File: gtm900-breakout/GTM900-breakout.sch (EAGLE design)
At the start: 94 parts, among them J1 AUDIO-JACK3, K1 694108106102, T1 BC847, T2 BC847, T3 BC847, T4 BC847, U1 FH12A-40S-0.5SH(55), U2 MCP1827T-ADJE/ET, U3 MIC5366, U4 CP2105-GM, U5 IP4234CZ6, X4 MINI-USB-SHIELD-UX60-MB-5ST

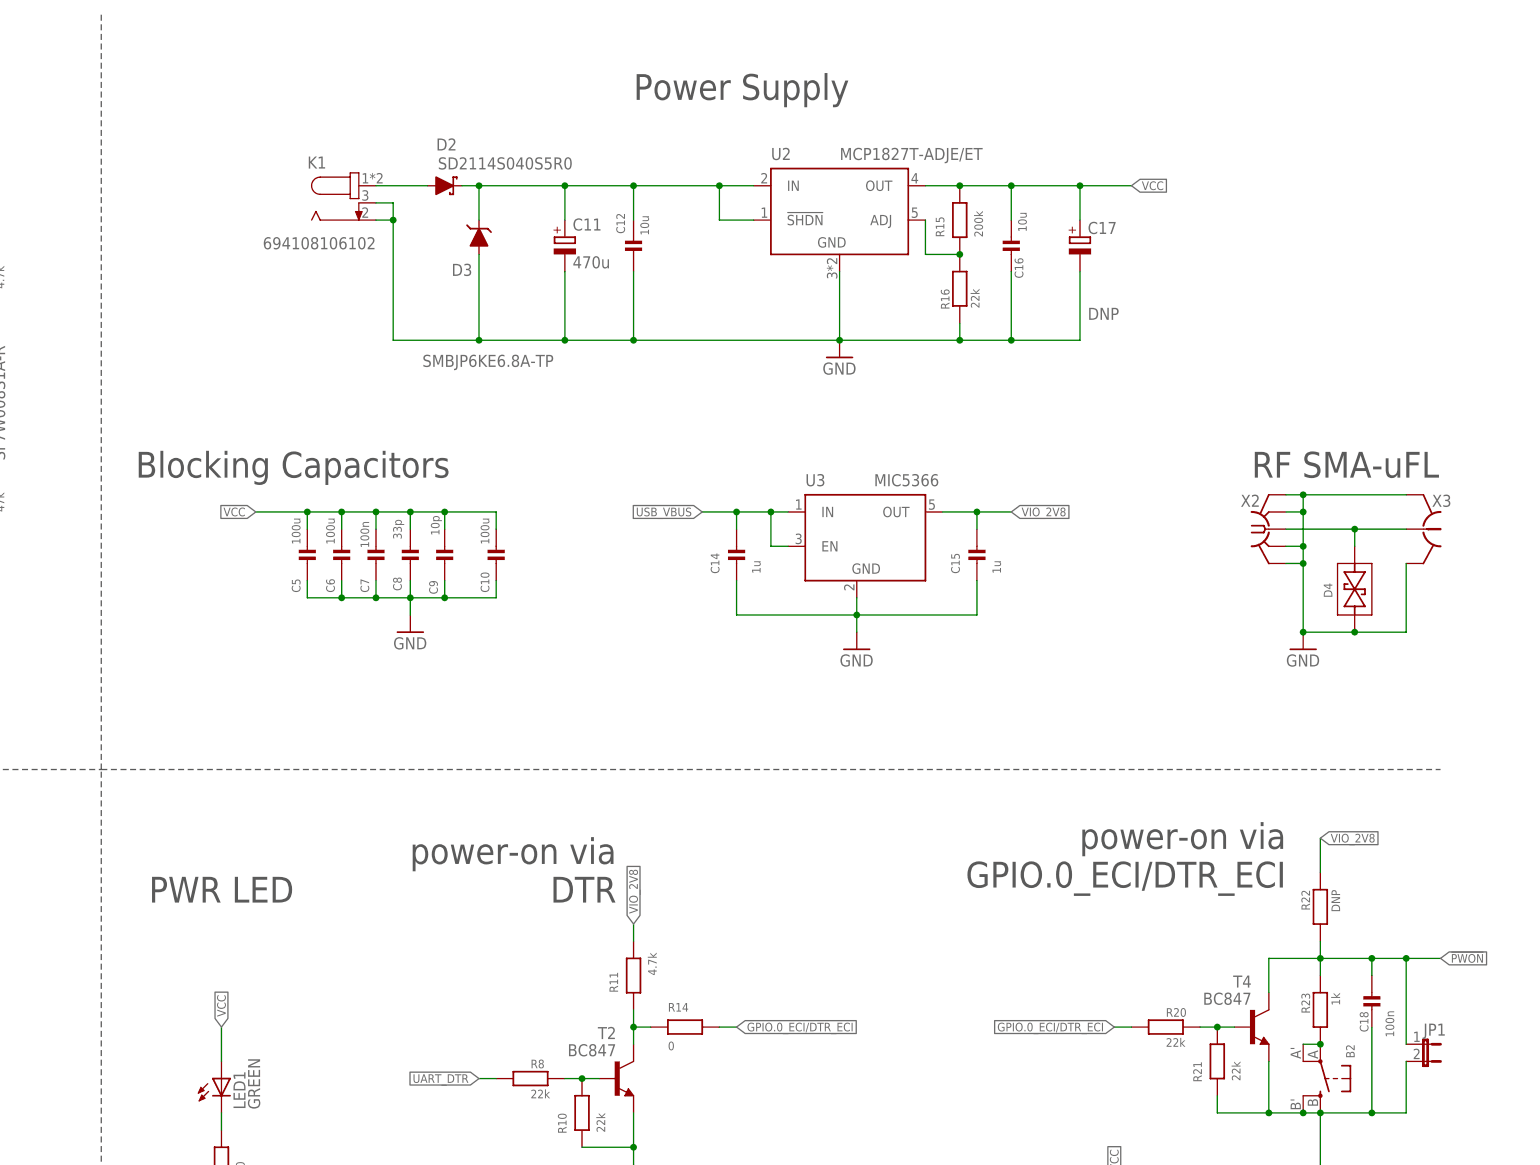
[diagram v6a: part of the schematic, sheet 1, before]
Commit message: gtm900-bo: add header for power source selection (DC in / USB)
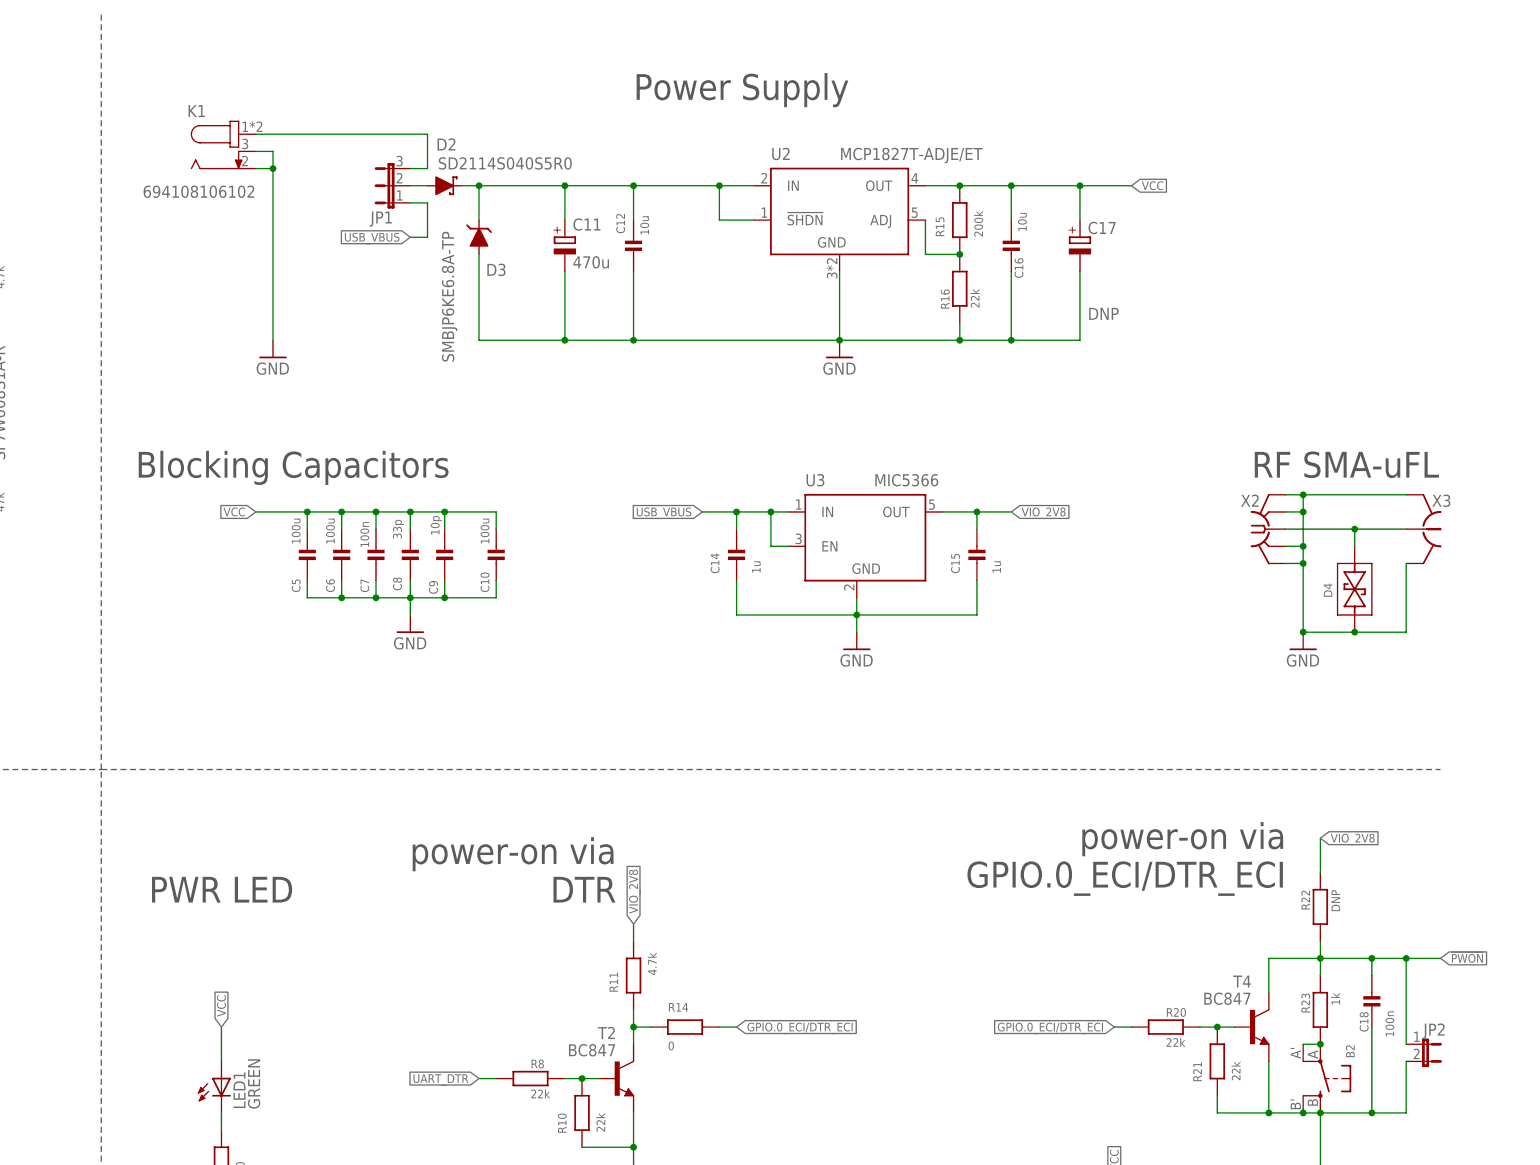
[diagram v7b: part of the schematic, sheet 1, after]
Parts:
- added JP3: (no value), microbuilder:HEADER-1X476MIL
- JP1: device jumper:JP1E -> jumper:JP2E
- JP2: device microbuilder:HEADER-1X476MIL -> jumper:JP1E
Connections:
- new net N$19: D2.A, JP1.2
- net !PWON: now also JP2.1; no longer JP1.1
- net EAR+: now also JP3.3; no longer JP2.3
- net EAR-: now also JP3.4; no longer JP2.4
- net GND: now also JP2.2; no longer JP1.2
- net MIC+: now also JP3.1; no longer JP2.1
- net MIC-: now also JP3.2; no longer JP2.2
- net N$4: now also JP1.3; no longer D2.A
- net USB_VBUS: now also JP1.1
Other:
- moved on the sheet: K1

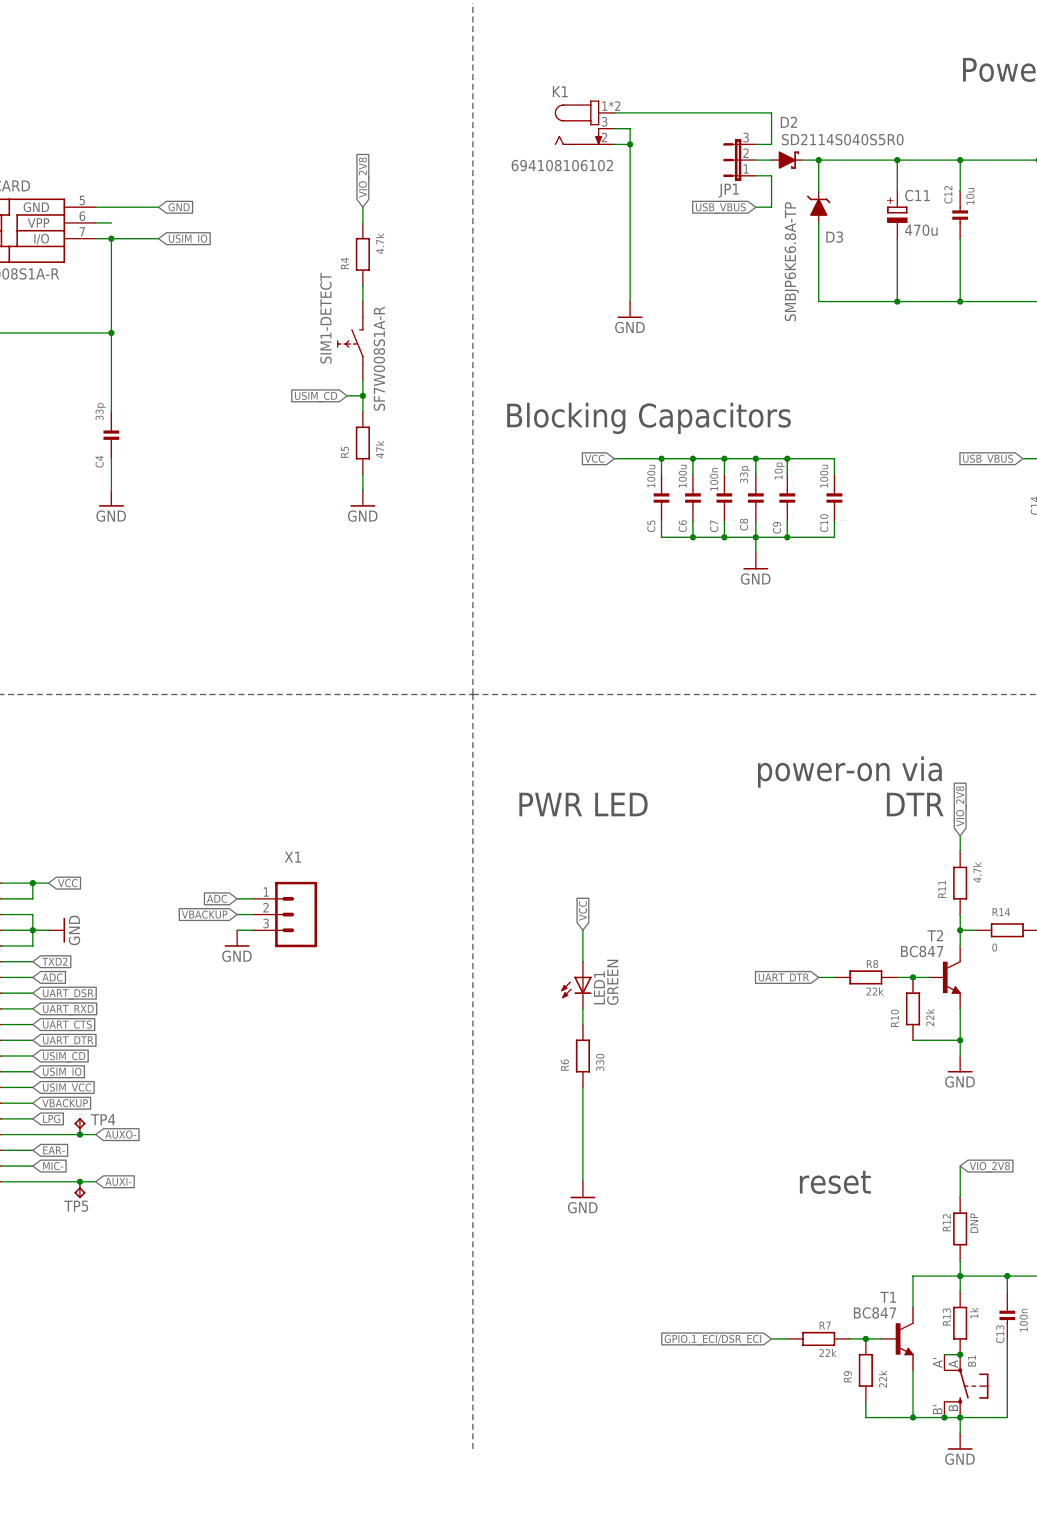
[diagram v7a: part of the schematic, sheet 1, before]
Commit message: gtm900-bo: update parts to avail @Digikey, upd all ext'd attribs
... in sch and brd too
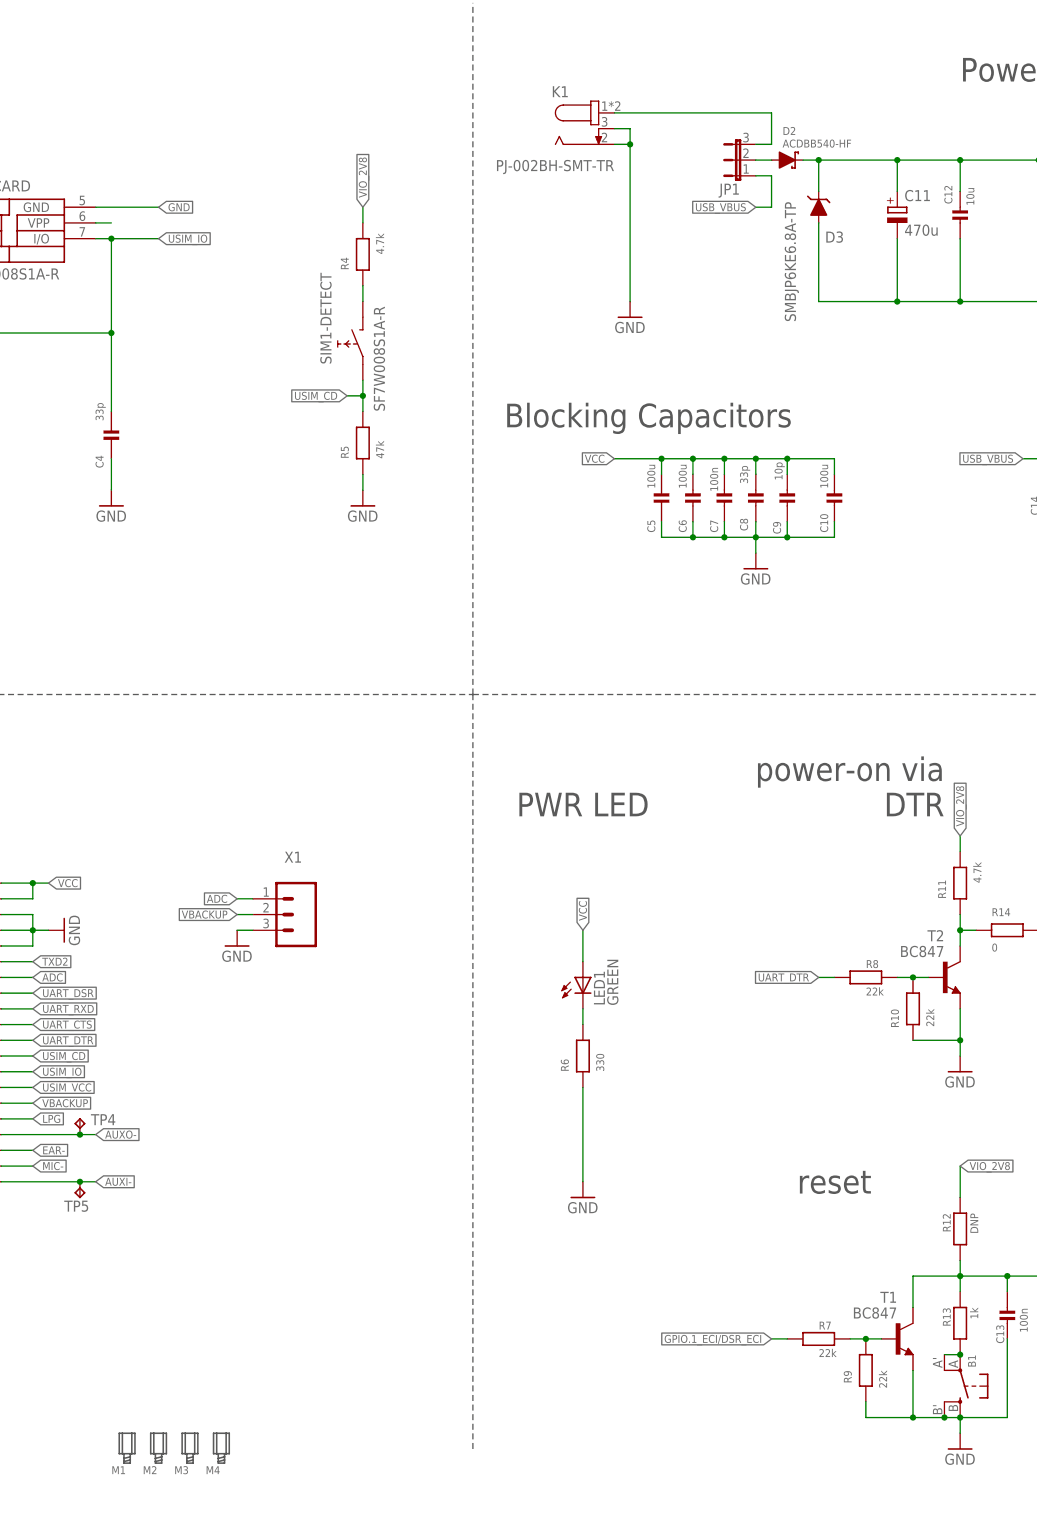
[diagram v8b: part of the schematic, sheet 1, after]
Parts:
- B1, B2: CLASS UNKNOWN CLASS -> TACT SWITCH; DESCRIPTION NO DESCRIPTION -> SWITCH TACTILE SPST-NO 0.02A 15V; LINK UNKNOWN LINK -> https://www.digikey.de/product-detail/de/panasonic-electron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; MANUFACTURER UNKNOWN MANUFACTURER -> Panasonic Electronic Components; MANUFACTURERPARTNUMBER UNKNOWN MANUFACTURER PART NUMBER -> EVQ-Q2M03W; SOURCE UNKNOWN SOURCE -> DIGIKEY; SOURCEPARTNUMBER UNKNOWN SOURCE PART NUMBER -> P12946SCT-ND
- C1, C13, C18, C7: LINK http://www.digikey.com/product-detail/en/foo/1276-1005-1-ND -> http://www.digikey.de/product-detail/de/foo/1276-1005-1-ND
- C10, C5, C6: DESCRIPTION 100µF 6.3V Ceramic Capacitor X5R 1206 (3216 Metric) 0.126" 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 -> CAP CER 100UF 6.3V X5R 1206; LINK http://www.digikey.com/product-detail/en/murata-electronics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 -> http://www.digikey.de/product-detail/de/murata-electronics-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; MANUFACTURER Murata Electronics North America -> Murata Electronics
- C11: DESCRIPTION 470µF 6.3V Aluminum Capacitors Radial, Can - SMD 2000 Hrs @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 -> CAP ALUM 470UF 20%% 6.3V SMD; LINK http://www.digikey.com/product-detail/en/nichicon/UUR0J471M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 -> http://www.digikey.de/product-detail/de/nichicon/UUR0J471MN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
- C12, C16, C31, C32: DESCRIPTION 10µF 16V Ceramic Capacitor X5R 0805 (2012 Metric) 0.079" L 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 -> CAP CER 10UF 16V X5R 0805; LINK http://www.digikey.com/product-detail/en/samsung-electro-me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 -> https://www.digikey.de/product-detail/de/murata-electronics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; MANUFACTURER Samsung Electro-Mechanics America, Inc. -> Murata Electronics; MANUFACTURERPARTNUMBER CL21A106KOQNNNG -> GRM21BR61C106KE15K; SOURCEPARTNUMBER 1276-6455-1-ND -> 490-6473-1-ND
- C14, C15, C20: DESCRIPTION 1µF 16V Ceramic Capacitor X5R 0603 (1608 Metric) 0.063" L x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 -> CAP CER 1UF 16V X5R 0603; LINK http://www.digikey.com/product-detail/en/murata-electronics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 -> https://www.digikey.de/product-detail/de/samsung-electro-me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; MANUFACTURER Murata Electronics North America -> Samsung Electro-Mechanics; MANUFACTURERPARTNUMBER GRM188R61C105KA93J -> CL10A105KO8NNNC; SOURCEPARTNUMBER 490-6412-1-ND -> 1276-1034-1-ND
- C19, C23: DESCRIPTION 4.7µF 10V Ceramic Capacitor X5R 0603 (1608 Metric) 0.063" L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 -> CAP CER 4.7UF 10V X5R 0603; LINK http://www.digikey.com/product-detail/en/samsung-electro-me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 -> https://www.digikey.de/product-detail/de/samsung-electro-me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; MANUFACTURER Samsung Electro-Mechanics America, Inc. -> Samsung Electro-Mechanics; MANUFACTURERPARTNUMBER CL10A475KP8NNNC -> CL10A475MP8NNNC; SOURCEPARTNUMBER 1276-1044-1-ND -> 1276-1905-1-ND
- C2, C25, C26, C27, C28, C29, C3, C30, C33, C34, C4, C8: LINK http://www.digikey.com/product-detail/en/CL05C330JB5NNNC/12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 -> http://www.digikey.de/product-detail/de/CL05C330JB5NNNC/127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
- C21, C22, C24: DESCRIPTION 0.10µF 16V Ceramic Capacitor X5R 0201 (0603 Metric) 0.024" 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 -> CAP CER 0.1UF 16V X5R 0201; LINK http://www.digikey.com/product-detail/en/murata-electronics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 -> http://www.digikey.de/product-detail/de/murata-electronics-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; MANUFACTURER Murata Electronics North America -> Murata Electronics
- C9: LINK http://www.digikey.com/product-detail/en/C0603C100J5GACTU/3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 -> http://www.digikey.de/product-detail/de/C0603C100J5GACTU/39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
- D2: value SD2114S040S5R0 -> ACDBB540-HF; DESCRIPTION DIODE SCHOTTKY 40V 5A SMB -> DIODE SCHOTTKY 40V 5A DO214AA; LINK https://www.digikey.de/product-detail/de/avx-corporation/SD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 -> https://www.digikey.de/product-detail/de/comchip-technology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; MANUFACTURER AVX Corporation -> Comchip Technology; MANUFACTURERPARTNUMBER SD2114S040S5R0 -> ACDBB540-HF; SOURCEPARTNUMBER 478-7816-1-ND -> 641-1898-2-ND
- D4: DESCRIPTION TVS DIODE 5V 10V 0402 -> TVS DIODE 5V 15.5V 0402; LINK https://www.digikey.de/product-detail/de/avx-corporation/GG040205170N2P/478-10595-1-ND/ -> https://www.digikey.de/product-detail/de/avx-corporation/GG0402050R3C2P/478-10591-1-ND; MANUFACTURERPARTNUMBER GG040205170N2P -> GG0402050R3C2P; ROHSCERTIFICATE Bleifrei / RoHS-konform -> UNKNOWN ROHS CERTIFICATE; SOURCEPARTNUMBER 478-10595-1-ND -> 478-10591-1-ND
- J1: CLASS (none) -> CONNECTOR; DESCRIPTION (none) -> AUDIO JACK, 3.5 MM, RT, 4 CONDUC; LINK (none) -> https://www.digikey.de/product-detail/de/cui-devices/SJ2-35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; MANUFACTURER (none) -> CUI Devices; MANUFACTURERPARTNUMBER (none) -> SJ2-3574A-SMT-TR; POPULATED (none) -> TRUE; ROHSCERTIFICATE (none) -> UNKNOWN ROHS CERTIFICATE; SOURCE (none) -> DIGIKEY; SOURCEPARTNUMBER (none) -> CP-SJ2-3574A-SMT-CT-ND
- K1: value 694108106102 -> PJ-002BH-SMT-TR; CLASS RELAY -> CONNECTOR; DESCRIPTION Power Barrel Connector Jack 2.50mm ID (0.098"), 5.50mm OD (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 -> CONN PWR JACK 2.5X5.5MM SOLDER; LINK http://www.digikey.com/product-detail/en/wurth-electronics-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 -> https://www.digikey.de/product-detail/de/cui-inc/PJ-002BH-S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; MANUFACTURER Wurth Electronics Inc -> CUI Devices; MANUFACTURERPARTNUMBER 694108106102 -> PJ-002BH-SMT-TR; SOURCEPARTNUMBER 732-5933-1-ND -> CP-002BHPJCT-ND
- R10, R16, R17, R18, R20, R21, R7, R8, R9: DESCRIPTION RES 22K OHM 1/10W 1% 0603 SMD -> RES SMD 22K OHM 1%% 1/10W 0603; LINK http://www.digikey.de/product-detail/de/MCR03ERTF2202/RHM22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 -> https://www.digikey.de/product-detail/de/yageo/RC0603FR-072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; MANUFACTURER Rohm Semiconductor -> Yageo; MANUFACTURERPARTNUMBER MCR03ERTF2202 -> RC0603FR-0722KL; ROHSCERTIFICATE Bleifrei / RoHS-konform -> UNKNOWN ROHS CERTIFICATE; SOURCEPARTNUMBER RHM22.0KCFCT-ND -> 311-22.0KHRCT-ND
- R11, R25, R4: DESCRIPTION RES SMD 4.7K OHM 5% 1/10W 0603 -> RES SMD 4.7K OHM 5%% 1/10W 0603; LINK http://www.digikey.com/product-detail/en/yageo/RC0603JR-074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 -> http://www.digikey.de/product-detail/de/yageo/RC0603JR-074K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
- R12, R22: POPULATED TRUE -> FALSE
- R13, R23: DESCRIPTION NO DESCRIPTION -> RES SMD 1K OHM 0.5%% 1/16W 0603; LINK UNKNOWN LINK -> https://www.digikey.de/product-detail/de/susumu/RR0816P-102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; MANUFACTURER UNKNOWN MANUFACTURER -> Susumu; MANUFACTURERPARTNUMBER UNKNOWN MANUFACTURER PART NUMBER -> RR0816P-102-D; SOURCE UNKNOWN SOURCE -> DIGIKEY; SOURCEPARTNUMBER UNKNOWN SOURCE PART NUMBER -> RR08P1.0KDCT-ND
- R14, R24, R27: DESCRIPTION NO DESCRIPTION -> RES 0 OHM JUMPER 1/16W 0402; LINK http://www.digikey.de/product-detail/de/AC0402JR-070RL/311-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 -> https://www.digikey.de/product-detail/de/stackpole-electron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; MANUFACTURER UNKNOWN MANUFACTURER -> Stackpole Electronics Inc; MANUFACTURERPARTNUMBER UNKNOWN MANUFACTURER PART NUMBER -> RMCF0402ZT0R00; SOURCE UNKNOWN SOURCE -> DIGIKEY; SOURCEPARTNUMBER UNKNOWN SOURCE PART NUMBER -> RMCF0402ZT0R00CT-ND
- R19, R6: DESCRIPTION RES SMD 330 OHM 5% 1/10W 0603 -> RES SMD 330 OHM 5%% 1/10W 0603; LINK http://www.digikey.com/product-detail/en/yageo/RC0603JR-073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 -> http://www.digikey.de/product-detail/de/yageo/RC0603JR-0733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
- R2, R3: DESCRIPTION RES SMD 47 OHM 5% 1/10W 0603 -> RES SMD 47 OHM 5%% 1/10W 0603; LINK http://www.digikey.com/product-detail/en/yageo/RC0603JR-074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 -> http://www.digikey.de/product-detail/de/yageo/RC0603JR-0747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
- R26: DESCRIPTION RES SMD 1M OHM 5% 1/20W 0201 -> RES SMD 1M OHM 1%% 1/10W 0603; LINK http://www.digikey.com/product-detail/en/samsung-electro-me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 -> https://www.digikey.de/product-detail/de/yageo/RC0603FR-071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; MANUFACTURER Samsung Electro-Mechanics America, Inc. -> Yageo; MANUFACTURERPARTNUMBER RC0603J105CS -> RC0603FR-071ML; SOURCEPARTNUMBER 1276-3856-1-ND -> 311-1.00MHRCT-ND
- R5: DESCRIPTION NO DESCRIPTION -> RES SMD 47K OHM 1%% 1/10W 0603; LINK https://www.digikey.de/product-detail/de/stackpole-electron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 -> https://www.digikey.de/product-detail/de/yageo/RC0603FR-074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; MANUFACTURER UNKNOWN MANUFACTURER -> Yageo; MANUFACTURERPARTNUMBER UNKNOWN MANUFACTURER PART NUMBER -> RC0603FR-0747KL; SOURCE UNKNOWN SOURCE -> DIGIKEY; SOURCEPARTNUMBER UNKNOWN SOURCE PART NUMBER -> 311-47.0KHRCT-ND
- SIM1: DESCRIPTION 8 (6 + 2) Position Card Connector SIM Card Surface Mount, R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 -> CONN SIM CARD HINGED TYPE R/A; LINK http://www.digikey.com/product-detail/en/jae-electronics/SF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 -> https://www.digikey.de/product-detail/de/jae-electronics/SF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; MANUFACTURERPARTNUMBER SF7W008S1AE900 -> SF7W008S1AR900; SOURCEPARTNUMBER 670-2337-1-ND -> 670-2985-1-ND
- T1, T2, T3, T4: CLASS UNKNOWN CLASS -> TRANSISTOR
- U1: CLASS IC -> CONNECTOR; DESCRIPTION NO DESCRIPTION -> CONN FFC TOP 40POS 0.50MM R/A; LINK UNKNOWN LINK -> https://www.digikey.de/product-detail/de/hirose-electric-co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; MANUFACTURER UNKNOWN MANUFACTURER -> Hirose Electric Co Ltd; MANUFACTURERPARTNUMBER UNKNOWN MANUFACTURER PART NUMBER -> FH12A-40S-0.5SH(55); SOURCE UNKNOWN SOURCE -> DIGIKEY; SOURCEPARTNUMBER UNKNOWN SOURCE PART NUMBER -> HFK140CT-ND
- U2: DESCRIPTION Linear Voltage Regulator IC Positive Fixed 1 Output 3.3V 3A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 -> IC REG LINEAR 3.3V 3A D2PAK; LINK http://www.digikey.com/product-detail/en/stmicroelectronics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 -> http://www.digikey.de/product-detail/de/stmicroelectronics/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
- U3: DESCRIPTION NO DESCRIPTION -> IC REG LINEAR 2.8V 150MA SC70-5; MANUFACTURER UNKNOWN MANUFACTURER -> Microchip Technology; MANUFACTURERPARTNUMBER UNKNOWN MANUFACTURER PART NUMBER -> MIC5366-2.8YC5-TR; SOURCE UNKNOWN SOURCE -> DIGIKEY; SOURCEPARTNUMBER UNKNOWN SOURCE PART NUMBER -> 576-3209-1-ND
- U4: DESCRIPTION USB Bridge, USB to UART USB 2.0 UART Interface 24-QFN (4x4) -> IC SGL USB-DL UART BRIDGE 24QFN; LINK http://www.digikey.com/product-detail/en/silicon-labs/CP210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 -> http://www.digikey.de/product-detail/de/silicon-labs/CP2105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
- U5: DESCRIPTION TVS DIODE 5.5VWM 6TSOP -> TVS DIODE 5.5V 6TSOP; LINK http://www.digikey.com/product-detail/en/nxp-semiconductors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 -> http://www.digikey.de/product-detail/de/nxp-semiconductors/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; MANUFACTURER NXP Semiconductors -> Nexperia USA Inc.; SOURCEPARTNUMBER 568-5869-1-ND -> 1727-4717-1-ND
- X1: CLASS (none) -> CONNECTOR; DESCRIPTION (none) -> NO DESCRIPTION; LINK (none) -> UNKNOWN LINK; MANUFACTURER (none) -> UNKNOWN MANUFACTURER; MANUFACTURERPARTNUMBER (none) -> UNKNOWN MANUFACTURER PART NUMBER; POPULATED (none) -> TRUE; ROHSCERTIFICATE (none) -> UNKNOWN ROHS CERTIFICATE; SOURCE (none) -> UNKNOWN SOURCE; SOURCEPARTNUMBER (none) -> UNKNOWN SOURCE PART NUMBER
- X2: LINK http://www.digikey.com/product-detail/en/te-connectivity-am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 -> http://www.digikey.de/product-detail/de/te-connectivity-amp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
- X3: CLASS UNKNOWN CLASS -> CONNECTOR; DESCRIPTION CONN UMC RCPT STR 50 OHM SMD -> CONN U.FL RCPT STR 50 OHM SMD; LINK http://www.digikey.com/product-detail/en/hirose-electric-co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 -> http://www.digikey.de/product-detail/de/hirose-electric-co-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
- X4: DESCRIPTION USB - mini B USB 2.0 Receptacle Connector 5 Position Surfac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 -> CONN RCPT USB2.0 MINI B SMD R/A; LINK http://www.digikey.com/product-detail/en/hirose-electric-co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 -> http://www.digikey.de/product-detail/de/hirose-electric-co-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
